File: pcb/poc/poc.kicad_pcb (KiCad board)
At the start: 2 copper layers, 0 parts

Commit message: pcb: poc: Some routing
Signed-off-by: Nikita Leshenko <nikita@leshenko.net>
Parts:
- added C1: CP, Capacitor_Tantalum_SMD:CP_EIA-3216-18_Kemet-A_Pad1.58x1.35mm_HandSolder, F.Cu at (73.0, 76.4)
- added C2: 22p, Capacitor_SMD:C_0805_2012Metric_Pad1.18x1.45mm_HandSolder, F.Cu at (84.2, 91.9)
- added C3: 22p, Capacitor_SMD:C_0805_2012Metric_Pad1.18x1.45mm_HandSolder, F.Cu at (84.3, 86.9)
- added C4: 1u, Capacitor_SMD:C_0805_2012Metric_Pad1.18x1.45mm_HandSolder, F.Cu at (96.6, 78.3)
- added C5: 100n, Capacitor_SMD:C_0805_2012Metric_Pad1.18x1.45mm_HandSolder, F.Cu at (97.0, 98.9)
- added C6: 100n, Capacitor_SMD:C_0805_2012Metric_Pad1.18x1.45mm_HandSolder, F.Cu at (91.3, 82.6)
- added C7: 100n, Capacitor_SMD:C_0805_2012Metric_Pad1.18x1.45mm_HandSolder, F.Cu at (109.0, 94.4)
- added C8: 100n, Capacitor_SMD:C_0805_2012Metric_Pad1.18x1.45mm_HandSolder, F.Cu at (100.5, 80.4)
- added C9: 100n, Capacitor_SMD:C_0805_2012Metric_Pad1.18x1.45mm_HandSolder, F.Cu at (110.0, 85.4)
- added D1: PRTR5V0U2X, Package_TO_SOT_SMD:SOT-143, F.Cu at (80.8, 69.2)
- added D10: LED_Small, LED_SMD:LED_0805_2012Metric_Pad1.15x1.40mm_HandSolder, F.Cu at (230.4, -9.30)
- added D11: D_Small, Diode_SMD:D_SOD-123, F.Cu at (247.8, -11.7)
- added D12: D_Small, Diode_SMD:D_SOD-123, F.Cu at (215.2, -73.3)
- added D13: D_Small, Diode_SMD:D_SOD-123, F.Cu at (245.7, -19.0)
- added D14: D_Small, Diode_SMD:D_SOD-123, F.Cu at (223.9, -84.5)
- added D2: D_Small, Diode_SMD:D_SOD-123, F.Cu at (76.7, 102.0)
- added D3: PRTR5V0U2X, Package_TO_SOT_SMD:SOT-143, F.Cu at (91.0, 65.1)
- added D4: LED_Small, LED_SMD:LED_0805_2012Metric_Pad1.15x1.40mm_HandSolder, F.Cu at (76.9, 78.1)
- added D5: PRTR5V0U2X, Package_TO_SOT_SMD:SOT-143, F.Cu at (206.3, -13.2)
- added D6: D_Small, Diode_SMD:D_SOD-123, F.Cu at (101.7, 122.0)
- added D7: D_Small, Diode_SMD:D_SOD-123, F.Cu at (111.0, 136.0)
- added D8: D_Small, Diode_SMD:D_SOD-123, F.Cu at (124.5, 121.5)
- added D9: D_Small, Diode_SMD:D_SOD-123, F.Cu at (123.0, 136.0)
- added F1: 500mA, Fuse:Fuse_0805_2012Metric_Pad1.15x1.40mm_HandSolder, F.Cu at (73.1, 69.5)
- added J1: USB_B_Mini, local_footprint:USB_Mini-B_Custom1_Horizontal, F.Cu at (73.9, 65.1)
- added J2: Right, local_footprint:RJ12_Custom1, F.Cu at (99.5, 57.5)
- added J3: Left, local_footprint:RJ12_Custom1, F.Cu at (224.0, -34.1)
- added J4: AVR-ISP-6, Connector_PinHeader_2.54mm:PinHeader_2x03_P2.54mm_Vertical, F.Cu at (76.1, 87.9)
- added J5: Conn_02x11_Odd_Even, Connector_PinSocket_2.54mm:PinSocket_2x11_P2.54mm_Vertical, F.Cu at (139.0, 65.0)
- added J6: Conn_02x06_Odd_Even, Connector_PinHeader_2.54mm:PinHeader_2x06_P2.54mm_Vertical, F.Cu at (263.3, -91.4)
- added R1: 22, Resistor_SMD:R_0805_2012Metric_Pad1.20x1.40mm_HandSolder, F.Cu at (103.5, 78.7)
- added R10: 10K, Resistor_SMD:R_0805_2012Metric_Pad1.20x1.40mm_HandSolder, F.Cu at (249.5, -63.7)
- added R11: R_Small, Resistor_SMD:R_0805_2012Metric_Pad1.20x1.40mm_HandSolder, F.Cu at (226.4, -66.8)
- added R12: R_Small, Resistor_SMD:R_0805_2012Metric_Pad1.20x1.40mm_HandSolder, F.Cu at (245.7, -74.2)
- added R13: 470, Resistor_SMD:R_0805_2012Metric_Pad1.20x1.40mm_HandSolder, F.Cu at (233.5, -95.0)
- added R14: 10K, Resistor_SMD:R_0805_2012Metric_Pad1.20x1.40mm_HandSolder, F.Cu at (214.1, -62.9)
- added R15: 10K, Resistor_SMD:R_0805_2012Metric_Pad1.20x1.40mm_HandSolder, F.Cu at (249.5, -54.8)
- added R2: 22, Resistor_SMD:R_0805_2012Metric_Pad1.20x1.40mm_HandSolder, F.Cu at (105.7, 78.8)
- added R3: 10K, Resistor_SMD:R_0805_2012Metric_Pad1.20x1.40mm_HandSolder, F.Cu at (76.0, 104.8)
- added R4: 10K, Resistor_SMD:R_0805_2012Metric_Pad1.20x1.40mm_HandSolder, F.Cu at (104.5, 99.4)
- added R5: 470, Resistor_SMD:R_0805_2012Metric_Pad1.20x1.40mm_HandSolder, F.Cu at (80.5, 79.1)
- added R6: 4.7K, Resistor_SMD:R_0805_2012Metric_Pad1.20x1.40mm_HandSolder, F.Cu at (91.0, 60.8)
- added R7: 4.7K, Resistor_SMD:R_0805_2012Metric_Pad1.20x1.40mm_HandSolder, F.Cu at (91.0, 58.0)
- added R8: 10K, Resistor_SMD:R_0805_2012Metric_Pad1.20x1.40mm_HandSolder, F.Cu at (92.5, 110.9)
- added R9: 10K, Resistor_SMD:R_0805_2012Metric_Pad1.20x1.40mm_HandSolder, F.Cu at (98.3, 111.7)
- added SW1: SW_Push, Button_Switch_THT:SW_PUSH_6mm_H4.3mm, F.Cu at (72.7, 98.7)
- added SW10: SW_Push_45deg, Button_Switch_Keyboard:SW_Cherry_MX_1.00u_PCB, F.Cu at (143.0, 116.5)
- added SW11: SW_Push_45deg, Button_Switch_Keyboard:SW_Cherry_MX_1.00u_PCB, F.Cu at (268.7, -32.3)
- added SW2: SW_Push_45deg, Button_Switch_THT:SW_PUSH_6mm_H4.3mm, F.Cu at (106.0, 113.5)
- added SW3: SW_Push_45deg, Button_Switch_THT:SW_PUSH_6mm_H4.3mm, F.Cu at (106.0, 125.0)
- added SW4: SW_Push_45deg, Button_Switch_THT:SW_PUSH_6mm_H4.3mm, F.Cu at (118.0, 113.5)
- added SW5: SW_Push_45deg, Button_Switch_THT:SW_PUSH_6mm_H4.3mm, F.Cu at (118.0, 125.0)
- added SW6: SW_Push_45deg, Button_Switch_THT:SW_PUSH_6mm_H4.3mm, F.Cu at (258.2, -55.3)
- added SW7: SW_Push_45deg, Button_Switch_THT:SW_PUSH_6mm_H4.3mm, F.Cu at (243.6, -35.5)
- added SW8: SW_Push_45deg, Button_Switch_THT:SW_PUSH_6mm_H4.3mm, F.Cu at (265.9, -66.7)
- added SW9: SW_Push_45deg, Button_Switch_THT:SW_PUSH_6mm_H4.3mm, F.Cu at (255.5, -43.8)
- added U1: ATmega32U4-AU, Package_QFP:TQFP-44_10x10mm_P0.8mm, F.Cu at (100.5, 89.9)
- added U2: MCP23018_SO, Package_SO:SOIC-28W_7.5x17.9mm_P1.27mm, F.Cu at (244.2, -102.0)
- added Y1: 16MHz, Crystal:Crystal_HC49-U_Vertical, F.Cu at (88.2, 91.8)
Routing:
- net +5V: track 0.00 -> 158.8 mm
- net GND: track 0.00 -> 41.3 mm, vias 0 -> 9
- net /D-: track 0.00 -> 39.1 mm
- net /D+: track 0.00 -> 35.9 mm
- net /MOSI: track 0.00 -> 28.4 mm, vias 0 -> 1
- net /SCK: track 0.00 -> 26.3 mm, vias 0 -> 1
- net /RESET: track 0.00 -> 24.5 mm
- net /MISO: track 0.00 -> 24.1 mm, vias 0 -> 1
- net Net-(R5-Pad1): track 0.00 -> 21.5 mm, vias 0 -> 2
- net Net-(C3-Pad1): track 0.00 -> 11.8 mm
- net Net-(C2-Pad1): track 0.00 -> 11.7 mm
- net Net-(C4-Pad1): track 0.00 -> 7.90 mm
- net /D1-: track 0.00 -> 5.66 mm
- net Net-(F1-Pad2): track 0.00 -> 5.14 mm
- net /D1+: track 0.00 -> 5.08 mm
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- added copper zone on B.Cu, net GND
- added copper zone on F.Cu, net GND
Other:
- board outline added: 100 x 100 mm
- net class Default: clearance 0.5 -> 0.25
- net class Power: clearance 0.5 -> 0.25
- rule trace_clearance: 0.5 -> 0.25

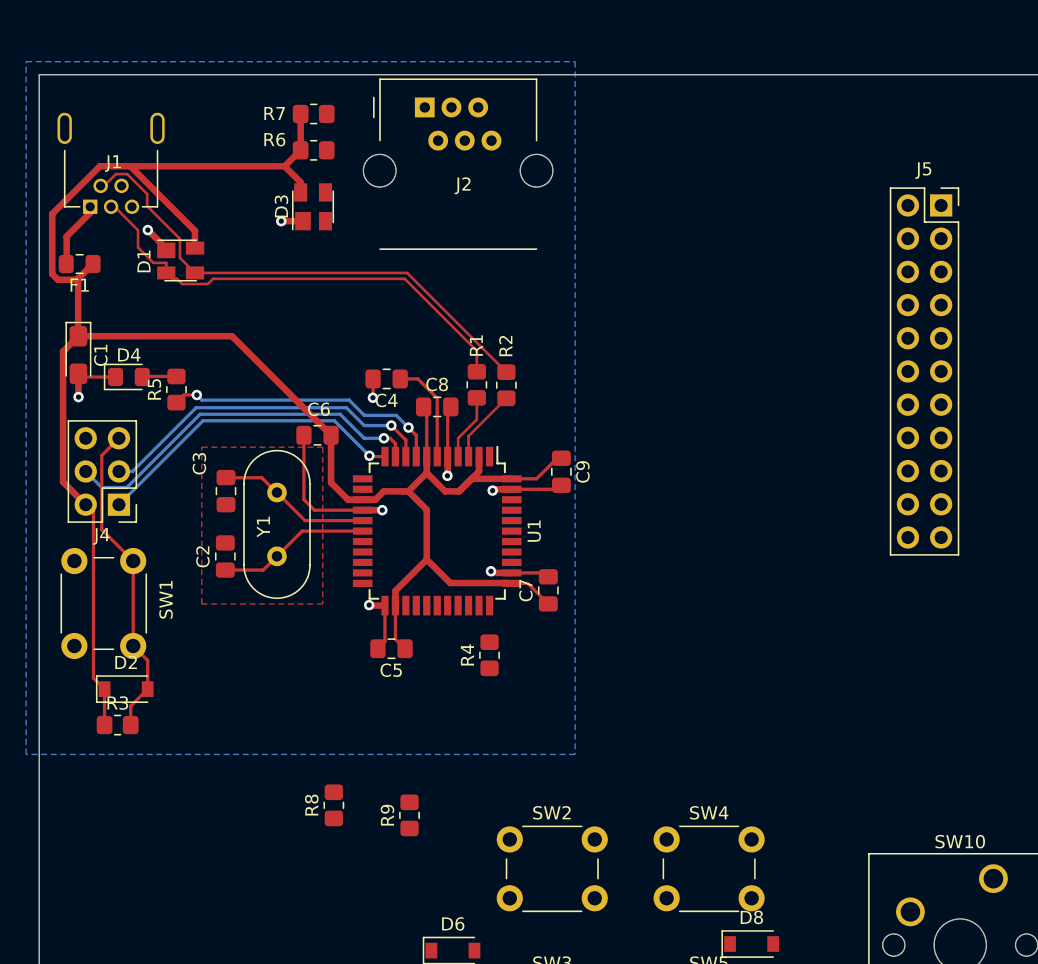
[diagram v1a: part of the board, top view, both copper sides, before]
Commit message: pcb: poc: Routed nabaz stuff
Signed-off-by: Nikita Leshenko <nikita@leshenko.net>
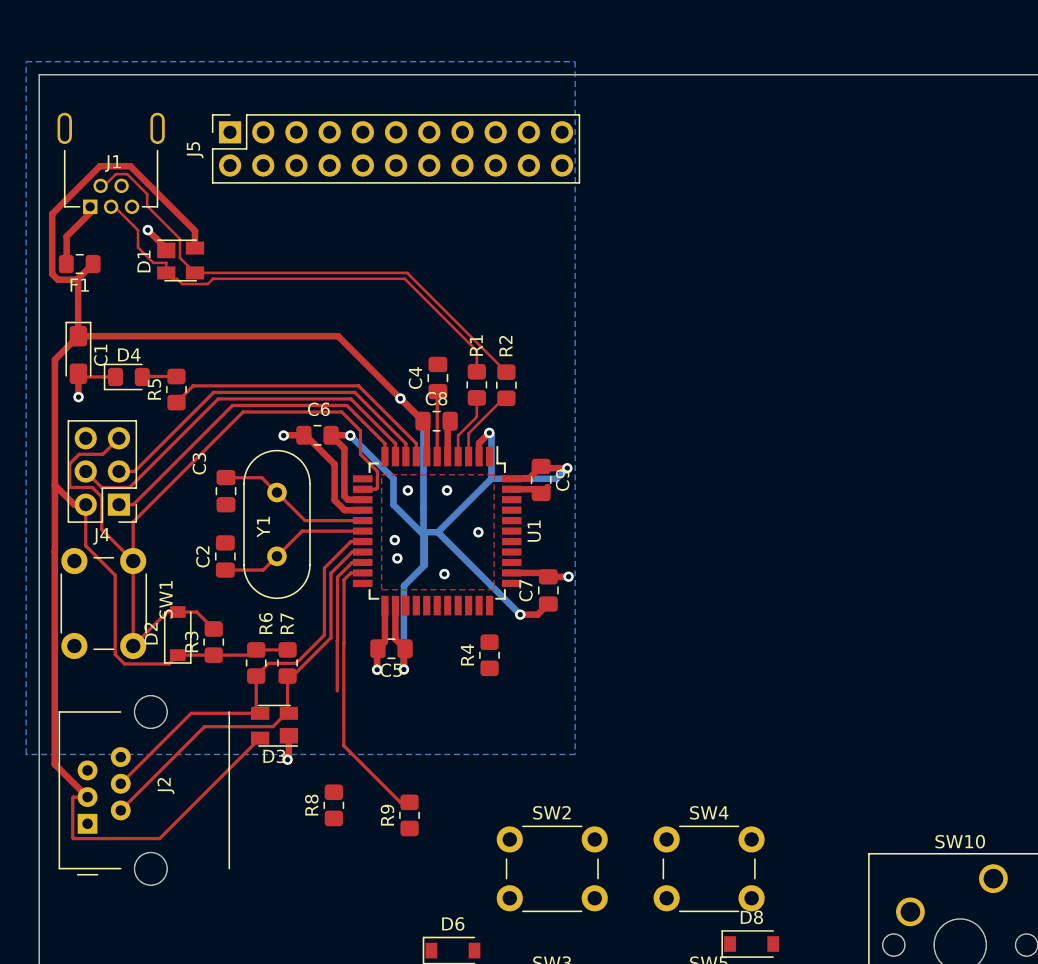
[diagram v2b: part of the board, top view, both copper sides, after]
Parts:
- moved J2 60.6 mm to (73.7, 112.3), turned to 90 degrees
- moved J5 54.7 mm to (84.6, 59.4), turned to 90 degrees
- moved R7 42.0 mm to (89.0, 100.0), turned to 270 degrees
- moved D3 39.8 mm to (88.0, 104.8), turned to 180 degrees
- moved R6 39.5 mm to (86.6, 100.0), turned to 270 degrees
- moved R3 9.71 mm to (83.3, 98.4), turned to 90 degrees
- moved D2 5.80 mm to (80.6, 97.8), turned to 90 degrees
- moved C4 3.92 mm to (100.5, 78.2), turned to 90 degrees
- moved C9 1.67 mm to (108.4, 86.0)
- moved C8 1.09 mm to (100.4, 81.5)
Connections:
- D3 pad 2: /SCL -> /SDA
- D3 pad 3: /SDA -> /SCL
- J1 pad 4: (no net) -> Net-(J1-Pad4)
- J2 pad 1: (no net) -> Net-(J2-Pad1)
- J2 pad 2: +5V -> /SDA
- J2 pad 3: /SDA -> +5V
- J2 pad 6: (no net) -> Net-(J2-Pad6)
- J3 pad 1: (no net) -> Net-(J3-Pad1)
- J3 pad 4: /SDA1 -> +5VP
- J3 pad 5: +5VP -> /SDA1
- J3 pad 6: (no net) -> Net-(J3-Pad6)
- J5 pad 5: /PB7 -> Net-(J5-Pad5)
- U1 pad 12: /PB7 -> Net-(U1-Pad12)
- U1 pad 42: (no net) -> Net-(U1-Pad42)
- U2 pad 14: (no net) -> Net-(U2-Pad14)
- U2 pad 17: (no net) -> Net-(U2-Pad17)
- U2 pad 18: (no net) -> Net-(U2-Pad18)
- U2 pad 19: (no net) -> Net-(U2-Pad19)
- U2 pad 2: (no net) -> Net-(U2-Pad2)
- U2 pad 28: (no net) -> Net-(U2-Pad28)
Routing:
- net +5V: track 158.8 -> 231.2 mm, vias 0 -> 6
- net /RESET: track 24.5 -> 59.8 mm
- net /SDA: track 0.00 -> 31.4 mm
- net /SCL: track 0.00 -> 31.3 mm
- net /COL1: track 0.00 -> 21.2 mm
- net /COL0: track 0.00 -> 11.1 mm
- net GND: track 41.3 -> 33.8 mm, vias 9 -> 12
- net Net-(C4-Pad1): track 7.90 -> 4.99 mm
- net /MISO: track 24.1 -> 25.7 mm, vias 1 -> 0
- net /MOSI: track 28.4 -> 29.4 mm, vias 1 -> 0
- net /SCK: track 26.3 -> 27.1 mm, vias 1 -> 0
- net Net-(R5-Pad1): track 21.5 -> 21.7 mm, vias 2 -> 0

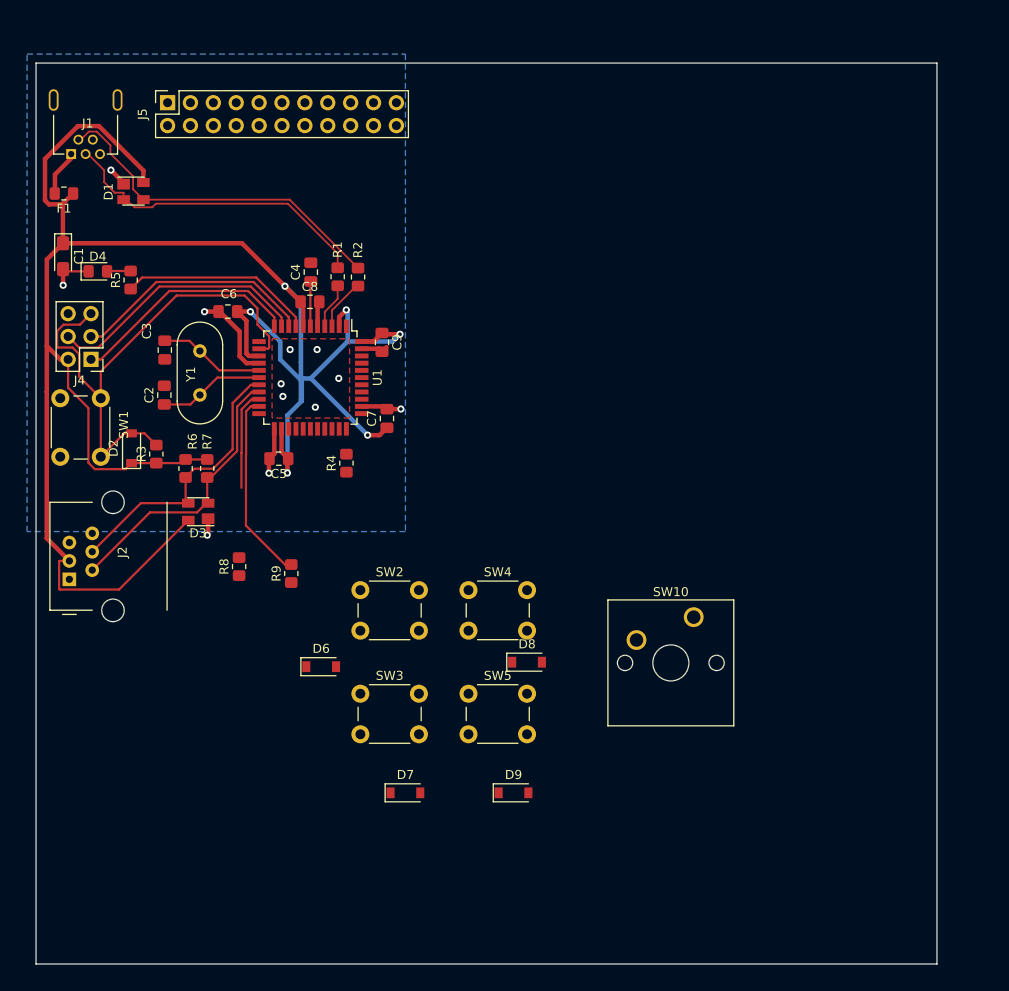
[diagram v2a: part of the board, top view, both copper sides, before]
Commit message: pcb: poc: Routed buttons and breakout
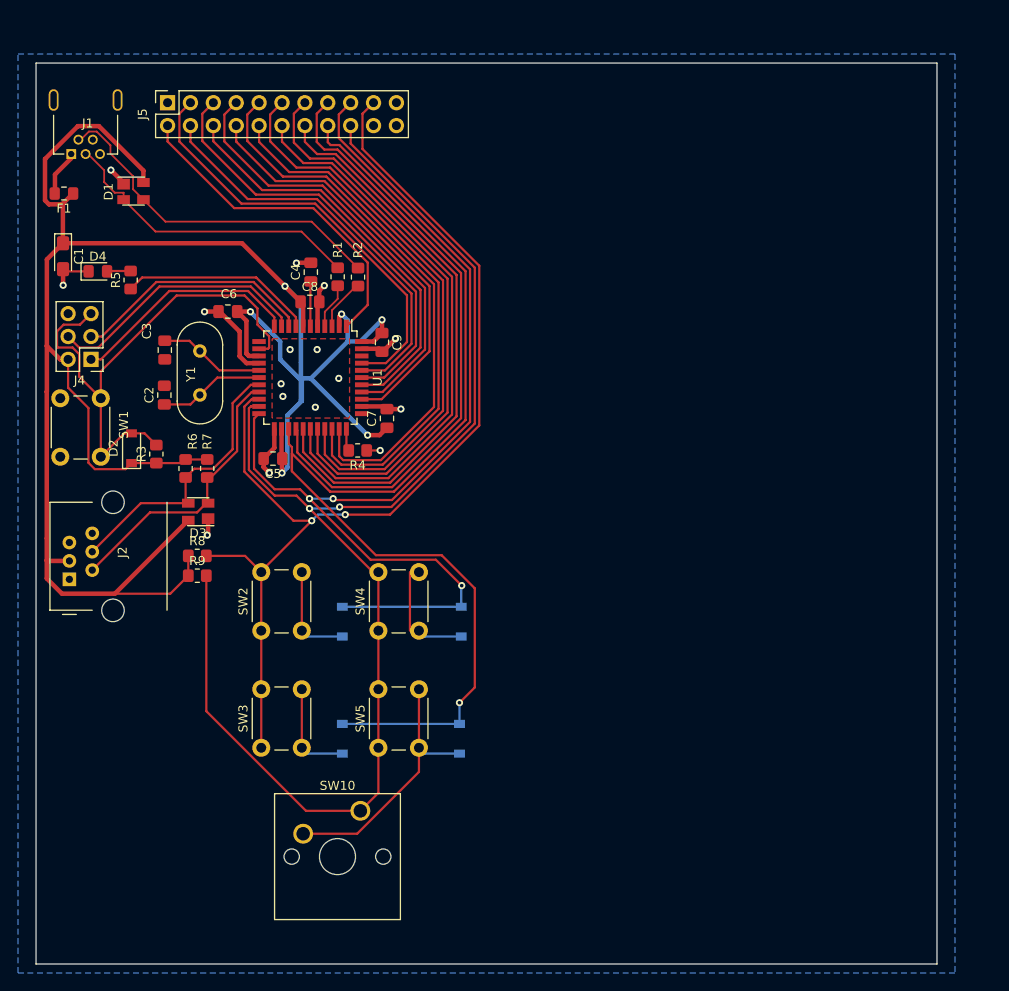
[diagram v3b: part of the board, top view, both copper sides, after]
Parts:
- D6, D7, D8, D9: moved to B.Cu
- moved SW10 42.8 mm to (106.0, 138.0)
- moved SW3 12.5 mm to (95.0, 131.0), turned to 90 degrees
- moved SW2 11.9 mm to (95.0, 118.0), turned to 90 degrees
- moved SW5 11.7 mm to (108.0, 131.0), turned to 90 degrees
- moved SW4 11.0 mm to (108.0, 118.0), turned to 90 degrees
- moved R9 10.4 mm to (87.9, 111.9), turned to 0 degrees
- moved D7 9.22 mm to (104.0, 130.0), turned to 270 degrees
- moved D8 8.58 mm to (117.2, 117.0), turned to 270 degrees
- moved D9 8.49 mm to (117.0, 130.0), turned to 270 degrees
- moved D6 5.52 mm to (104.0, 117.0), turned to 270 degrees
- moved R8 4.79 mm to (87.9, 109.7), turned to 0 degrees
- moved R4 1.88 mm to (105.7, 98.0), turned to 180 degrees
- moved C5 0.65 mm to (96.3, 98.9)
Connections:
- J5 pad 10: /PF4 -> /PC6
- J5 pad 11: /PD6 -> /PB6
- J5 pad 12: /PF5 -> /PB5
- J5 pad 13: /PD7 -> /PB4
- J5 pad 14: /PF6 -> /PD7
- J5 pad 15: /PE6 -> /PD6
- J5 pad 16: /PF7 -> /ROW1
- J5 pad 17: /SDA -> /ROW0
- J5 pad 18: /SCL -> /COL1
- J5 pad 19: /ROW0 -> /COL0
- J5 pad 2: /PC6 -> /PE6
- J5 pad 20: /COL0 -> /SDA
- J5 pad 21: /ROW1 -> /SCL
- J5 pad 22: /COL1 -> Net-(J5-Pad22)
- J5 pad 3: /PB6 -> /PF0
- J5 pad 4: /PC7 -> /PF1
- J5 pad 5: Net-(J5-Pad5) -> /PF4
- J5 pad 6: /PF0 -> /PF5
- J5 pad 7: /PD4 -> /PF6
- J5 pad 8: /PF1 -> /PF7
- J5 pad 9: /PD5 -> /PC7
- SW10 pad 2: Net-(D8-Pad2) -> Net-(D9-Pad2)
- U1 pad 22: /PD5 -> /ROW0
- U1 pad 25: /PD4 -> /ROW1
- U1 pad 28: /ROW0 -> /PB4
- U1 pad 29: /ROW1 -> /PB5
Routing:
- net /COL1: track 21.2 -> 152.2 mm, vias 0 -> 2
- net /ROW1: track 0.00 -> 125.2 mm, vias 0 -> 1
- net /ROW0: track 0.00 -> 113.9 mm, vias 0 -> 3
- net /COL0: track 11.1 -> 118.0 mm, vias 0 -> 2
- net /PD6: track 0.00 -> 68.6 mm
- net /PB4: track 0.00 -> 66.4 mm
- net /PD7: track 0.00 -> 64.5 mm
- net /PB6: track 0.00 -> 64.2 mm
- net /PB5: track 0.00 -> 62.2 mm
- net /PC7: track 0.00 -> 61.9 mm
- net /PC6: track 0.00 -> 60.0 mm
- net /PF6: track 0.00 -> 49.7 mm
- net /PF4: track 0.00 -> 48.9 mm
- net /PF0: track 0.00 -> 48.3 mm
- net /PF7: track 0.00 -> 46.8 mm
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
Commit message: pcb: poc: Change 2x11 to 2x10 breakout
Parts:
- J5: value Conn_02x11_Odd_Even -> Conn_02x10_Odd_Even; footprint Connector_PinSocket_2.54mm:PinSocket_2x11_P2.54mm_Vertical -> Connector_PinSocket_2.54mm:PinSocket_2x10_P2.54mm_Vertical
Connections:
- J5 pad 20: /SDA -> Net-(J5-Pad20)
